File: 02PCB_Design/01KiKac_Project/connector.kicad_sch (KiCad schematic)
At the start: 1 part, among them J5 MTSW-104-22-L-D-265-RA

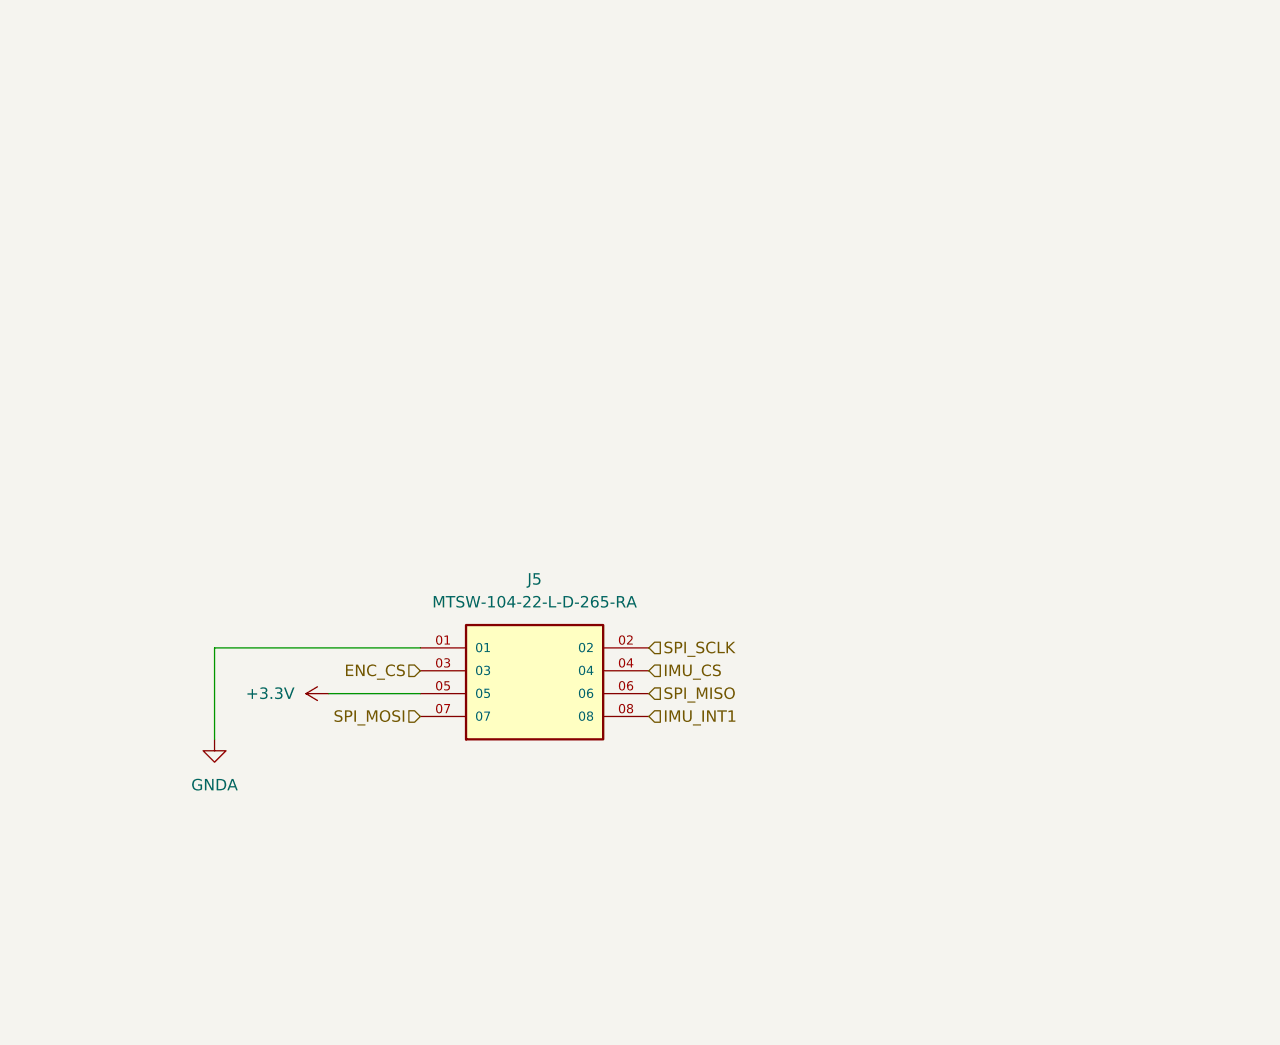
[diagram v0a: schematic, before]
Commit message: added CAN + minor changes
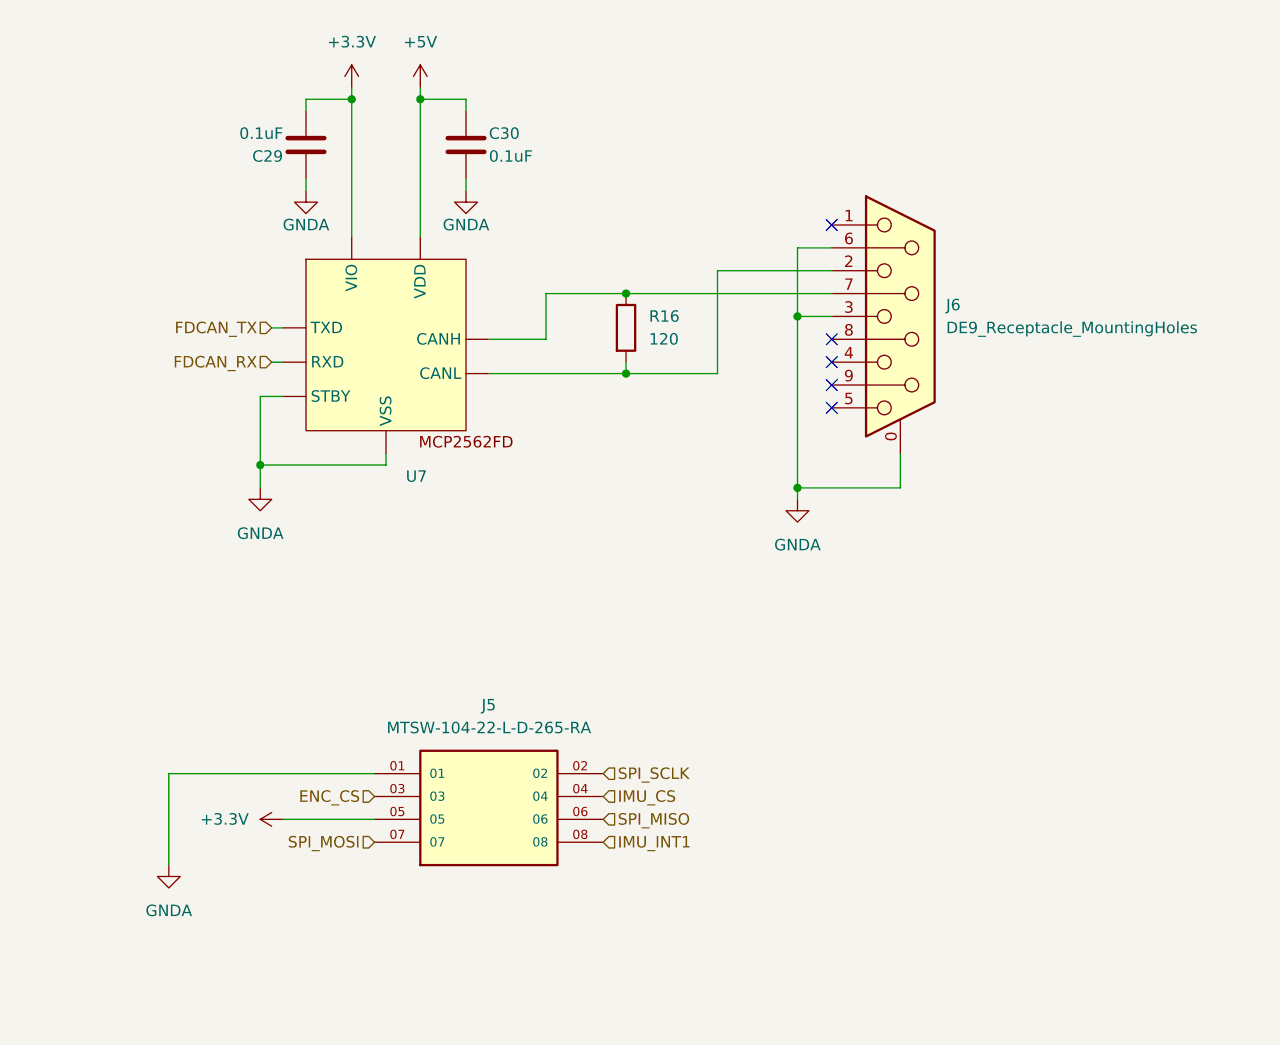
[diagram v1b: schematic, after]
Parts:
- added C29, C30: 0.1uF, symbol Device:C
- added J6: DE9_Receptacle_MountingHoles, symbol Connector:DE9_Receptacle_MountingHoles
- added R16: 120, symbol Device:R
- added U7: ~, symbol MyKiCadLib:MCP2562FD
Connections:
- net +3.3V: now also C29.2, U7. (VSS)
- net GNDA: now also C29.1, C30.2, J6.0 (PAD), J6.3, J6.6, U7. (VSS)
- new net: J6.7, R16.1, U7. (VSS)
- new net: J6.2, R16.2, U7. (VSS)
- new net +5V: C30.1, U7. (VSS)
- new net FDCAN_RX: U7. (VSS)
- new net FDCAN_TX: U7. (VSS)
- no-connect marks 0 -> 5
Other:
- moved on the sheet: J5

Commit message: cleanup
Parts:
- added J7: Conn_01x06_Pin, symbol Connector:Conn_01x06_Pin
- renumbered C29 to C69, C30 to C70, J6 to J5, J5 to J6, R16 to R40, U7 to U12
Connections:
- net +3.3V: now also J7.5 (Pin_5)
- net +5V: now also J7.6 (Pin_6)
- net GNDA: now also J7.1 (Pin_1)
- new net O_ENC_A: J7.2 (Pin_2)
- new net O_ENC_B: J7.3 (Pin_3)
- new net O_ENC_I: J7.4 (Pin_4)
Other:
- note added: "6-Pin 2.54mm Connector"
- note added: "8-Pin 2.54mm Connector"
- note added: "FDCAN Transceiver + DE9 Connector"
- note added: "To connect Optional Rotary Encoder"
- note added: "To connect Sensor and ESC PCB"
- moved on the sheet: C69, C70, J5, J6, R40, U12

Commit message: besprechung
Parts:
- renumbered R40 to R43
